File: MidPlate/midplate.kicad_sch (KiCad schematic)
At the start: 0 parts

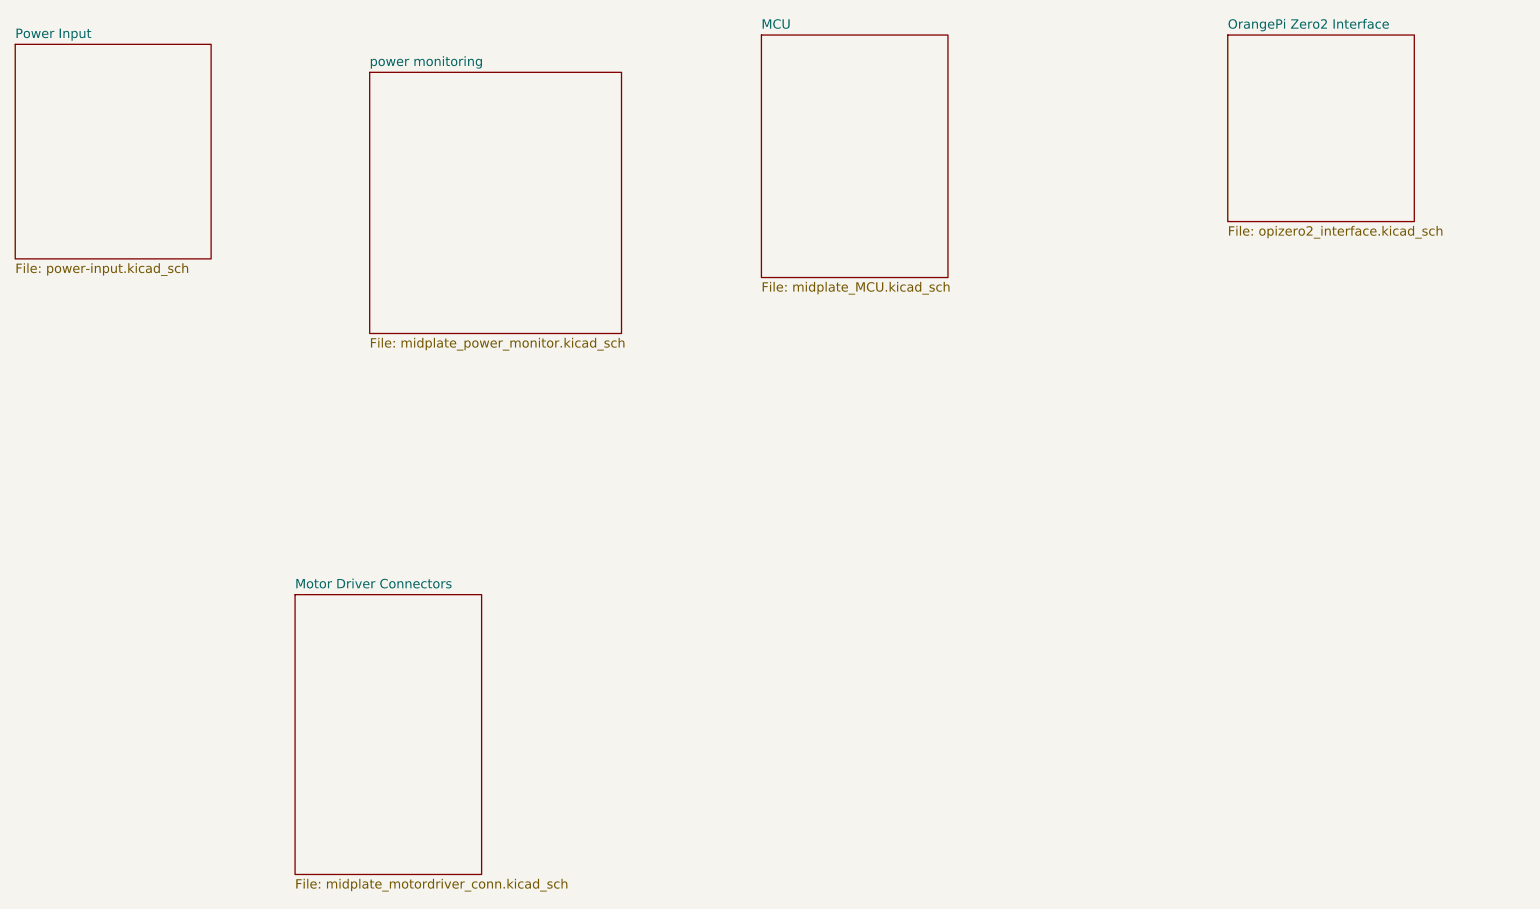
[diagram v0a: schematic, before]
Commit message: powerboard HV powerpillars + midplate
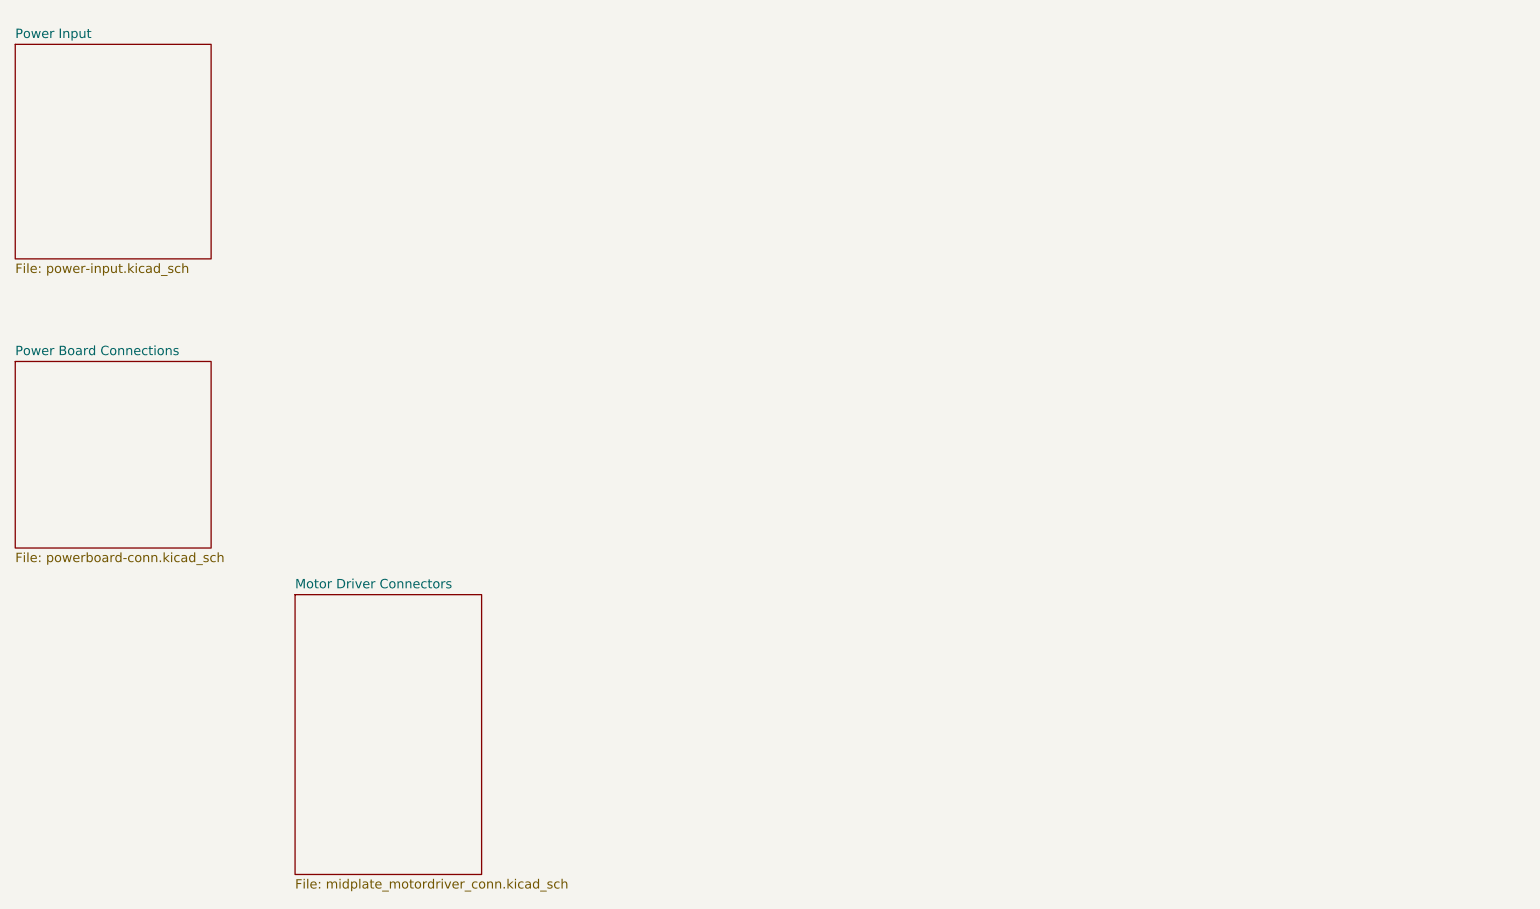
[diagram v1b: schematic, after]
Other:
- removed sheet MCU
- removed sheet OrangePi Zero2 Interface
- removed sheet power monitoring
- added sheet Power Board Connections (powerboard-conn.kicad_sch)
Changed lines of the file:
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@@
 (kicad_sch (version 20230121) (generator eeschema)
   (paper "A4")
-  (sheet (at 139.7 38.1) (size 25.4 33.02) (fields_autoplaced)
+  (sheet (at 38.1 82.55) (size 26.67 25.4) (fields_autoplaced)
     (stroke (width 0.1524) (type solid))
     (fill (color 0 0 0 0.0000))
-    (property "Sheetname" "MCU" (at 139.7 37.3884 0)
+    (property "Sheetname" "Power Board Connections" (at 38.1 81.8384 0)
       (effects (font (size 1.27 1.27)) (justify left bottom))
     )
-    (property "Sheetfile" "midplate_MCU.kicad_sch" (at 139.7 71.7046 0)
+    (property "Sheetfile" "powerboard-conn.kicad_sch" (at 38.1 108.5346 0)
       (effects (font (size 1.27 1.27)) (justify left top))
     )
@@
       (project "midplate"
         (path "/69058343-dac8-421b-a3f6-e069eb1ba8ae" (page "3"))
-      )
-    )
-  )
-  (sheet (at 203.2 38.1) (size 25.4 25.4) (fields_autoplaced)
-    (stroke (width 0.1524) (type solid))
-    (fill (color 0 0 0 0.0000))
-    (property "Sheetname" "OrangePi Zero2 Interface" (at 203.2 37.3884 0)
-      (effects (font (size 1.27 1.27)) (justify left bottom))
-    )
-    (property "Sheetfile" "opizero2_interface.kicad_sch" (at 203.2 64.0846 0)
-      (effects (font (size 1.27 1.27)) (justify left top))
-    )
-    (instances
-      (project "midplate"
-        (path "/69058343-dac8-421b-a3f6-e069eb1ba8ae" (page "5"))
-      )
-    )
-  )
-  (sheet (at 86.36 43.18) (size 34.29 35.56) (fields_autoplaced)
-    (stroke (width 0.1524) (type solid))
-    (fill (color 0 0 0 0.0000))
-    (property "Sheetname" "power monitoring" (at 86.36 42.4684 0)
-      (effects (font (size 1.27 1.27)) (justify left bottom))
-    )
-    (property "Sheetfile" "midplate_power_monitor.kicad_sch" (at 86.36 79.3246 0)
-      (effects (font (size 1.27 1.27)) (justify left top))
-    )
-    (instances
-      (project "midplate"
-        (path "/69058343-dac8-421b-a3f6-e069eb1ba8ae" (page "6"))
       )
     )
@@
   )
   (sheet_instances
-    (path "/" (page "1"))
+    (path "/" (page "7"))
   )
 )

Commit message: midplate mods
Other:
- removed sheet Motor Driver Connectors
- added sheet Faceplate Connections (faceplate.kicad_sch)
- added sheet Motor Driver Connections (motor.kicad_sch)
- added sheet Mounting Holes (mounting_holes.kicad_sch)
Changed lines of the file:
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@@
 (kicad_sch (version 20230121) (generator eeschema)
   (paper "A4")
-  (sheet (at 38.1 82.55) (size 26.67 25.4) (fields_autoplaced)
+  (sheet (at 73.66 40.64) (size 26.67 25.4) (fields_autoplaced)
     (stroke (width 0.1524) (type solid))
     (fill (color 0 0 0 0.0000))
-    (property "Sheetname" "Power Board Connections" (at 38.1 81.8384 0)
+    (property "Sheetname" "Power Board Connections" (at 73.66 39.9284 0)
       (effects (font (size 1.27 1.27)) (justify left bottom))
     )
-    (property "Sheetfile" "powerboard-conn.kicad_sch" (at 38.1 108.5346 0)
+    (property "Sheetfile" "powerboard-conn.kicad_sch" (at 73.66 66.6246 0)
       (effects (font (size 1.27 1.27)) (justify left top))
     )
@@
     )
   )
-  (sheet (at 38.1 39.37) (size 26.67 29.21) (fields_autoplaced)
+  (sheet (at 118.11 40.64) (size 21.59 27.94) (fields_autoplaced)
+    (stroke (width 0.1524) (type solid))
+    (fill (color 0 0 0 0.0000))
+    (property "Sheetname" "Motor Driver Connections" (at 118.11 39.9284 0)
+      (effects (font (size 1.27 1.27)) (justify left bottom))
+    )
+    (property "Sheetfile" "motor.kicad_sch" (at 118.11 69.1646 0)
+      (effects (font (size 1.27 1.27)) (justify left top))
+    )
+    (instances
+      (project "midplate"
+        (path "/69058343-dac8-421b-a3f6-e069eb1ba8ae" (page "4"))
+      )
+    )
+  )
+  (sheet (at 38.1 39.37) (size 22.86 27.94) (fields_autoplaced)
     (stroke (width 0.1524) (type solid))
     (fill (color 0 0 0 0.0000))
@@
       (effects (font (size 1.27 1.27)) (justify left bottom))
     )
-    (property "Sheetfile" "power-input.kicad_sch" (at 38.1 69.1646 0)
+    (property "Sheetfile" "power-input.kicad_sch" (at 38.1 67.8946 0)
       (effects (font (size 1.27 1.27)) (justify left top))
     )
@@
     )
   )
-  (sheet (at 76.2 114.3) (size 25.4 38.1) (fields_autoplaced)
+  (sheet (at 38.1 80.01) (size 22.86 26.67) (fields_autoplaced)
     (stroke (width 0.1524) (type solid))
     (fill (color 0 0 0 0.0000))
-    (property "Sheetname" "Motor Driver Connectors" (at 76.2 113.5884 0)
+    (property "Sheetname" "Mounting Holes" (at 38.1 79.2984 0)
       (effects (font (size 1.27 1.27)) (justify left bottom))
     )
-    (property "Sheetfile" "midplate_motordriver_conn.kicad_sch" (at 76.2 152.9846 0)
+    (property "Sheetfile" "mounting_holes.kicad_sch" (at 38.1 107.2646 0)
       (effects (font (size 1.27 1.27)) (justify left top))
     )
     (instances
       (project "midplate"
-        (path "/69058343-dac8-421b-a3f6-e069eb1ba8ae" (page "4"))
+        (path "/69058343-dac8-421b-a3f6-e069eb1ba8ae" (page "6"))
       )
     )
+  )
+  (sheet (at 157.48 40.64) (size 24.13 33.02) (fields_autoplaced)
+    (stroke (width 0.1524) (type solid))
+    (fill (color 0 0 0 0.0000))
+    (property "Sheetname" "Faceplate Connections" (at 157.48 39.9284 0)
+      (effects (font (size 1.27 1.27)) (justify left bottom))
+    )
+    (property "Sheetfile" "faceplate.kicad_sch" (at 157.48 74.2446 0)
+      (effects (font (size 1.27 1.27)) (justify left top))
+    )
+    (instances
+      (project "midplate"
+        (path "/69058343-dac8-421b-a3f6-e069eb1ba8ae" (page "5"))
+      )
+    )

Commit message: midplate thoughts
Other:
- sheet Motor Driver Connections renamed Baseplate Connections
- sheet Baseplate Connections: file motor.kicad_sch -> baseplate-conn.kicad_sch
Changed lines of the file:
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@@
     (stroke (width 0.1524) (type solid))
     (fill (color 0 0 0 0.0000))
-    (property "Sheetname" "Motor Driver Connections" (at 118.11 39.9284 0)
+    (property "Sheetname" "Baseplate Connections" (at 118.11 39.9284 0)
       (effects (font (size 1.27 1.27)) (justify left bottom))
     )
-    (property "Sheetfile" "motor.kicad_sch" (at 118.11 69.1646 0)
+    (property "Sheetfile" "baseplate-conn.kicad_sch" (at 118.11 69.1646 0)
       (effects (font (size 1.27 1.27)) (justify left top))
     )

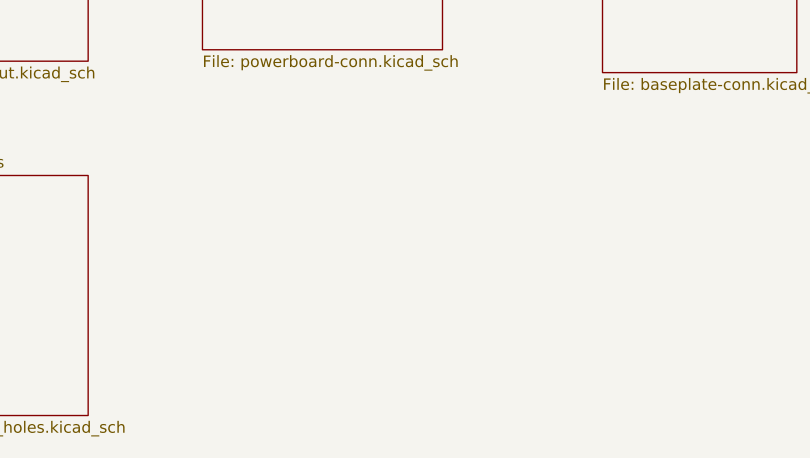
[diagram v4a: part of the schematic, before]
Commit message: midplate pass through
ethernet pass through
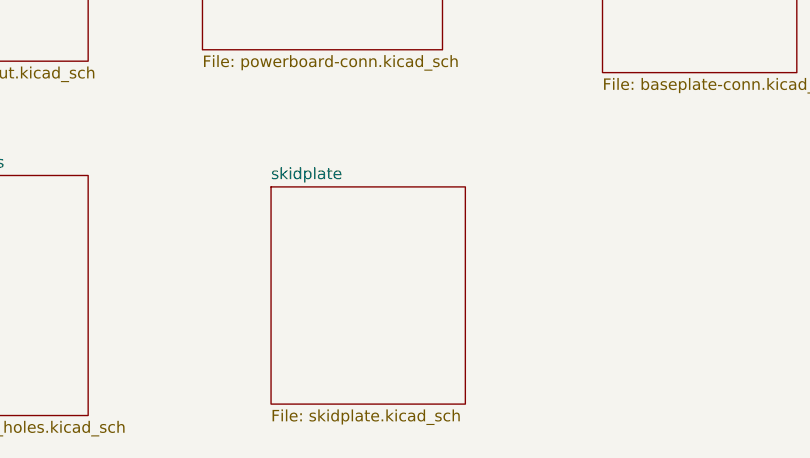
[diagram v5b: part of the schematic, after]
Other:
- added sheet skidplate (skidplate.kicad_sch)
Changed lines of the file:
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@@
 (kicad_sch
-	(version 20250114)
+	(version 20260306)
 	(generator "eeschema")
-	(generator_version "9.0")
+	(generator_version "10.0")
 	(paper "A4")
 	(sheet
@@
 		)
 		(fill
-			(color 0 0 0 0.0000)
+			(color 0 0 0 0)
 		)
 		(property "Sheetname" "Power Board Connections"
 			(at 73.66 39.9284 0)
+			(show_name no)
+			(do_not_autoplace no)
 			(effects
 				(font
@@
 		(property "Sheetfile" "powerboard-conn.kicad_sch"
 			(at 73.66 66.6246 0)
+			(show_name no)
+			(do_not_autoplace no)
 			(effects
 				(font
@@
 		)
 		(fill
-			(color 0 0 0 0.0000)
+			(color 0 0 0 0)
 		)
 		(property "Sheetname" "Baseplate Connections"
 			(at 118.11 39.9284 0)
+			(show_name no)
+			(do_not_autoplace no)
 			(effects
 				(font
@@
 		(property "Sheetfile" "baseplate-conn.kicad_sch"
 			(at 118.11 69.1646 0)
+			(show_name no)
+			(do_not_autoplace no)
 			(effects
 				(font
@@
 		)
 		(fill
-			(color 0 0 0 0.0000)
+			(color 0 0 0 0)
 		)
 		(property "Sheetname" "Power Input"
 			(at 38.1 38.6584 0)
+			(show_name no)
+			(do_not_autoplace no)
 			(effects
 				(font
@@
 		(property "Sheetfile" "power-input.kicad_sch"
 			(at 38.1 67.8946 0)
+			(show_name no)
+			(do_not_autoplace no)
 			(effects
 				(font
@@
 				(path "/69058343-dac8-421b-a3f6-e069eb1ba8ae"
 					(page "2")
+				)
+			)
+		)
+	)
+	(sheet
+		(at 81.28 81.28)
+		(size 21.59 24.13)
+		(exclude_from_sim no)
+		(in_bom yes)
+		(on_board yes)
+		(dnp no)
+		(fields_autoplaced yes)
+		(stroke
+			(width 0.1524)
+			(type solid)
+		)
+		(fill
+			(color 0 0 0 0)
+		)
+		(property "Sheetname" "skidplate"
+			(at 81.28 80.5684 0)
+			(show_name no)
+			(do_not_autoplace no)
+			(effects
+				(font
+					(size 1.27 1.27)
+				)
+				(justify left bottom)
+			)
+		)
+		(property "Sheetfile" "skidplate.kicad_sch"
+			(at 81.28 105.9946 0)
+			(show_name no)
+			(do_not_autoplace no)
+			(effects
+				(font
+					(size 1.27 1.27)
+				)
+				(justify left top)
+			)
+		)
+		(instances
+			(project "midplate"
+				(path "/69058343-dac8-421b-a3f6-e069eb1ba8ae"
+					(page "1")
 				)
 			)
@@
 		)
 		(fill
-			(color 0 0 0 0.0000)
+			(color 0 0 0 0)
 		)
 		(property "Sheetname" "Mounting Holes"
 			(at 38.1 79.2984 0)
+			(show_name no)
+			(do_not_autoplace no)
 			(effects
 				(font
@@
 		(property "Sheetfile" "mounting_holes.kicad_sch"
 			(at 38.1 107.2646 0)
+			(show_name no)
+			(do_not_autoplace no)
 			(effects
 				(font
@@
 		)
 		(fill
-			(color 0 0 0 0.0000)
+			(color 0 0 0 0)
 		)
 		(property "Sheetname" "Faceplate Connections"
 			(at 157.48 39.9284 0)
+			(show_name no)
+			(do_not_autoplace no)
 			(effects
 				(font
@@
 		(property "Sheetfile" "faceplate.kicad_sch"
 			(at 157.48 74.2446 0)
-			(effects
-				(font
+			(show_name no)
+			(do_not_autoplace no)
+			(effects
+				(font

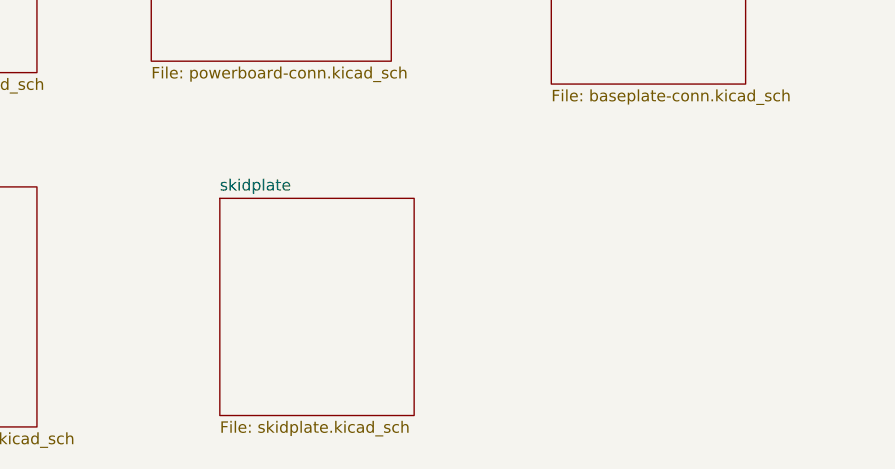
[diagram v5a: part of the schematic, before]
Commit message: add usb pd and imu to midplate
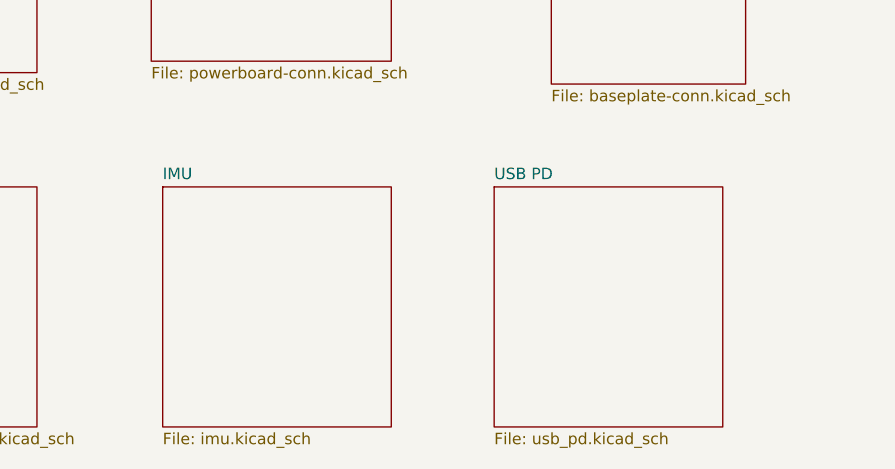
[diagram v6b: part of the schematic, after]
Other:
- removed sheet skidplate
- added sheet IMU (imu.kicad_sch)
- added sheet USB PD (usb_pd.kicad_sch)
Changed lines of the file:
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@@
 	(paper "A4")
+	(sheet
+		(at 74.93 80.01)
+		(size 25.4 26.67)
+		(exclude_from_sim no)
+		(in_bom yes)
+		(on_board yes)
+		(dnp no)
+		(fields_autoplaced yes)
+		(stroke
+			(width 0.1524)
+			(type solid)
+		)
+		(fill
+			(color 0 0 0 0)
+		)
+		(property "Sheetname" "IMU"
+			(at 74.93 79.2984 0)
+			(show_name no)
+			(do_not_autoplace no)
+			(effects
+				(font
+					(size 1.27 1.27)
+				)
+				(justify left bottom)
+			)
+		)
+		(property "Sheetfile" "imu.kicad_sch"
+			(at 74.93 107.2646 0)
+			(show_name no)
+			(do_not_autoplace no)
+			(effects
+				(font
+					(size 1.27 1.27)
+				)
+				(justify left top)
+			)
+		)
+		(instances
+			(project "midplate"
+				(path "/69058343-dac8-421b-a3f6-e069eb1ba8ae"
+					(page "1")
+				)
+			)
+		)
+	)
 	(sheet
 		(at 73.66 40.64)
@@
 	)
 	(sheet
+		(at 111.76 80.01)
+		(size 25.4 26.67)
+		(exclude_from_sim no)
+		(in_bom yes)
+		(on_board yes)
+		(dnp no)
+		(fields_autoplaced yes)
+		(stroke
+			(width 0.1524)
+			(type solid)
+		)
+		(fill
+			(color 0 0 0 0)
+		)
+		(property "Sheetname" "USB PD"
+			(at 111.76 79.2984 0)
+			(show_name no)
+			(do_not_autoplace no)
+			(effects
+				(font
+					(size 1.27 1.27)
+				)
+				(justify left bottom)
+			)
+		)
+		(property "Sheetfile" "usb_pd.kicad_sch"
+			(at 111.76 107.2646 0)
+			(show_name no)
+			(do_not_autoplace no)
+			(effects
+				(font
+					(size 1.27 1.27)
+				)
+				(justify left top)
+			)
+		)
+		(instances
+			(project "midplate"
+				(path "/69058343-dac8-421b-a3f6-e069eb1ba8ae"
+					(page "8")
+				)
+			)
+		)
+	)
+	(sheet
 		(at 38.1 39.37)
 		(size 22.86 27.94)
@@
 				)
 			)
-		)
-	)
-	(sheet
-		(at 81.28 81.28)
-		(size 21.59 24.13)
-		(exclude_from_sim no)
-		(in_bom yes)
-		(on_board yes)
-		(dnp no)
-		(fields_autoplaced yes)
-		(stroke
-			(width 0.1524)
-			(type solid)
-		)
-		(fill
-			(color 0 0 0 0)
-		)
-		(property "Sheetname" "skidplate"
-			(at 81.28 80.5684 0)
-			(show_name no)
-			(do_not_autoplace no)
-			(effects
-				(font
-					(size 1.27 1.27)
-				)
-				(justify left bottom)
-			)
-		)
-		(property "Sheetfile" "skidplate.kicad_sch"
-			(at 81.28 105.9946 0)
-			(show_name no)
-			(do_not_autoplace no)
-			(effects
-				(font
-					(size 1.27 1.27)
-				)
-				(justify left top)
-			)
-		)
-		(instances
-			(project "midplate"
-				(path "/69058343-dac8-421b-a3f6-e069eb1ba8ae"
-					(page "1")
-				)
-			)

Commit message: midplate additions WIP
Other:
- removed sheet USB PD
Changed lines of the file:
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@@
-	)
-	(sheet
-		(at 111.76 80.01)
-		(size 25.4 26.67)
-		(exclude_from_sim no)
-		(in_bom yes)
-		(on_board yes)
-		(dnp no)
-		(fields_autoplaced yes)
-		(stroke
-			(width 0.1524)
-			(type solid)
-		)
-		(fill
-			(color 0 0 0 0)
-		)
-		(property "Sheetname" "USB PD"
-			(at 111.76 79.2984 0)
-			(show_name no)
-			(do_not_autoplace no)
-			(effects
-				(font
-					(size 1.27 1.27)
-				)
-				(justify left bottom)
-			)
-		)
-		(property "Sheetfile" "usb_pd.kicad_sch"
-			(at 111.76 107.2646 0)
-			(show_name no)
-			(do_not_autoplace no)
-			(effects
-				(font
-					(size 1.27 1.27)
-				)
-				(justify left top)
-			)
-		)
-		(instances
-			(project "midplate"
-				(path "/69058343-dac8-421b-a3f6-e069eb1ba8ae"
-					(page "8")
-				)
-			)
-		)
 	)
 	(sheet

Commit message: skidplate and midplate
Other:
- removed sheet IMU
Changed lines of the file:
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@@
 	(paper "A4")
-	(sheet
-		(at 74.93 80.01)
-		(size 25.4 26.67)
-		(exclude_from_sim no)
-		(in_bom yes)
-		(on_board yes)
-		(dnp no)
-		(fields_autoplaced yes)
-		(stroke
-			(width 0.1524)
-			(type solid)
-		)
-		(fill
-			(color 0 0 0 0)
-		)
-		(property "Sheetname" "IMU"
-			(at 74.93 79.2984 0)
-			(show_name no)
-			(do_not_autoplace no)
-			(effects
-				(font
-					(size 1.27 1.27)
-				)
-				(justify left bottom)
-			)
-		)
-		(property "Sheetfile" "imu.kicad_sch"
-			(at 74.93 107.2646 0)
-			(show_name no)
-			(do_not_autoplace no)
-			(effects
-				(font
-					(size 1.27 1.27)
-				)
-				(justify left top)
-			)
-		)
-		(instances
-			(project "midplate"
-				(path "/69058343-dac8-421b-a3f6-e069eb1ba8ae"
-					(page "1")
-				)
-			)
-		)
-	)
 	(sheet
 		(at 73.66 40.64)
